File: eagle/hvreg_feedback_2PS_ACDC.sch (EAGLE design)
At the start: 20 parts

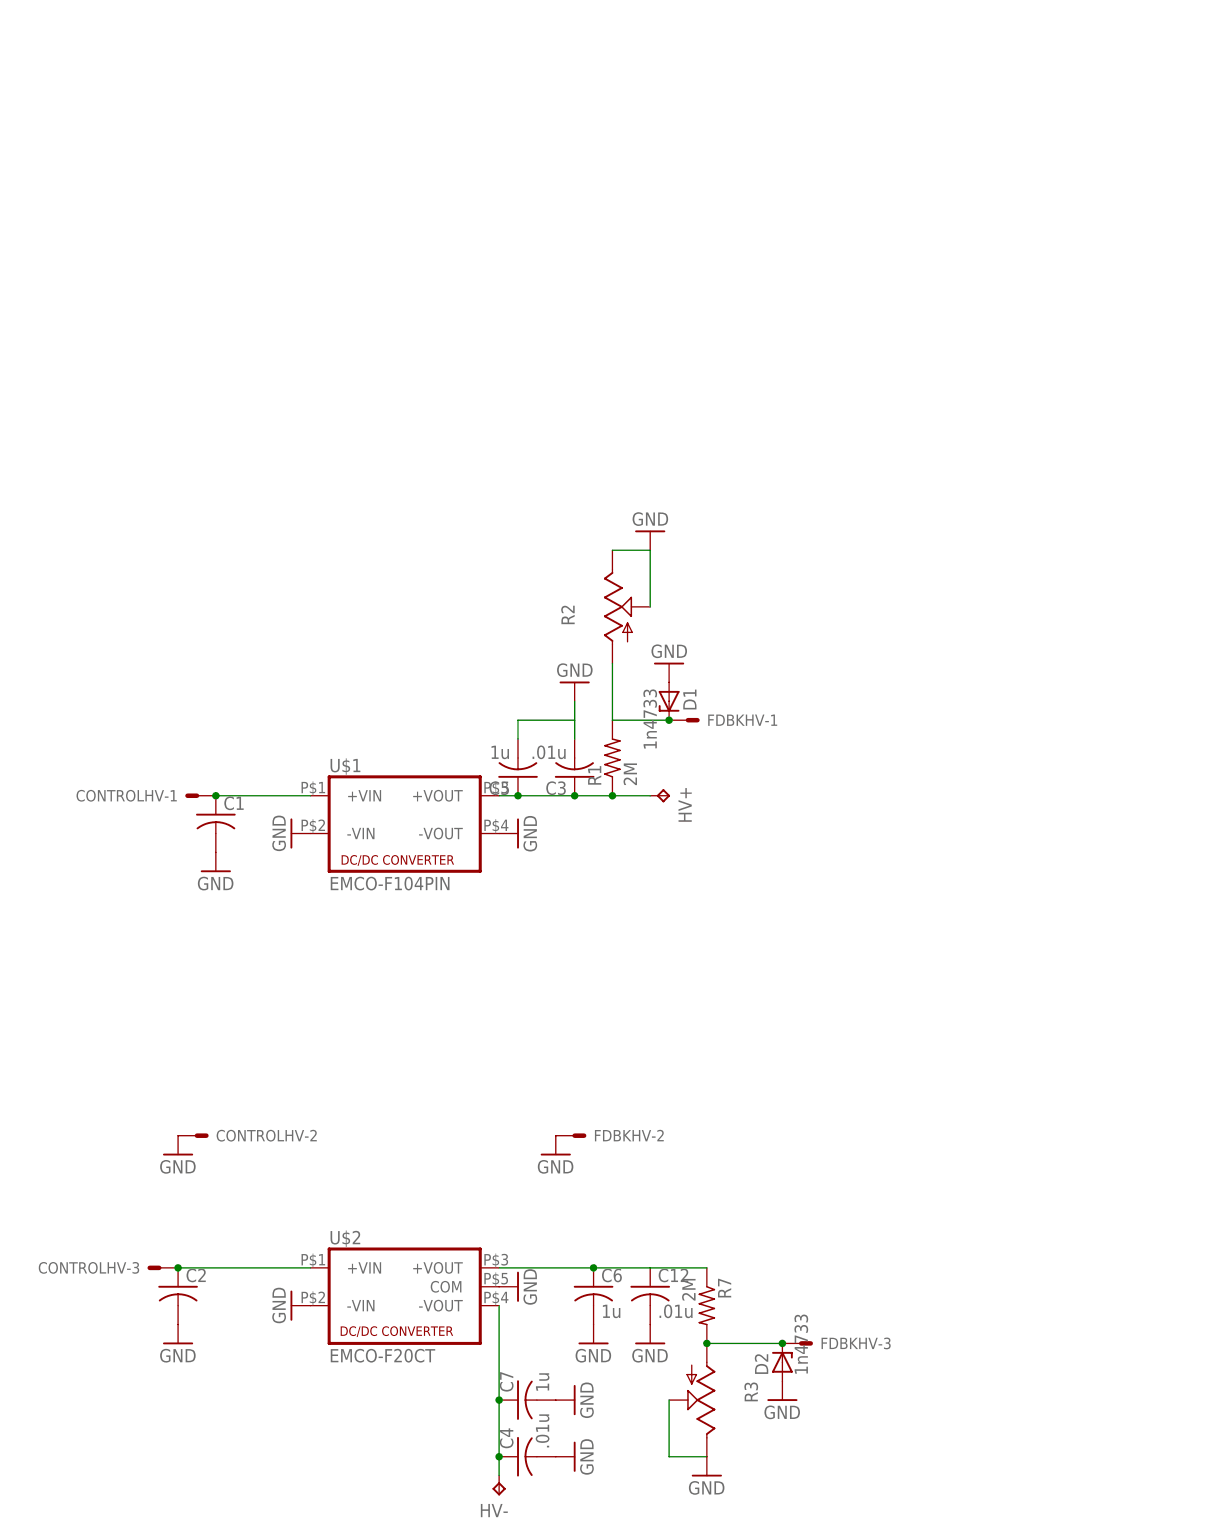
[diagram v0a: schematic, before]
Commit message: use SW on one side, DC on the other. HV feedback. Positive only
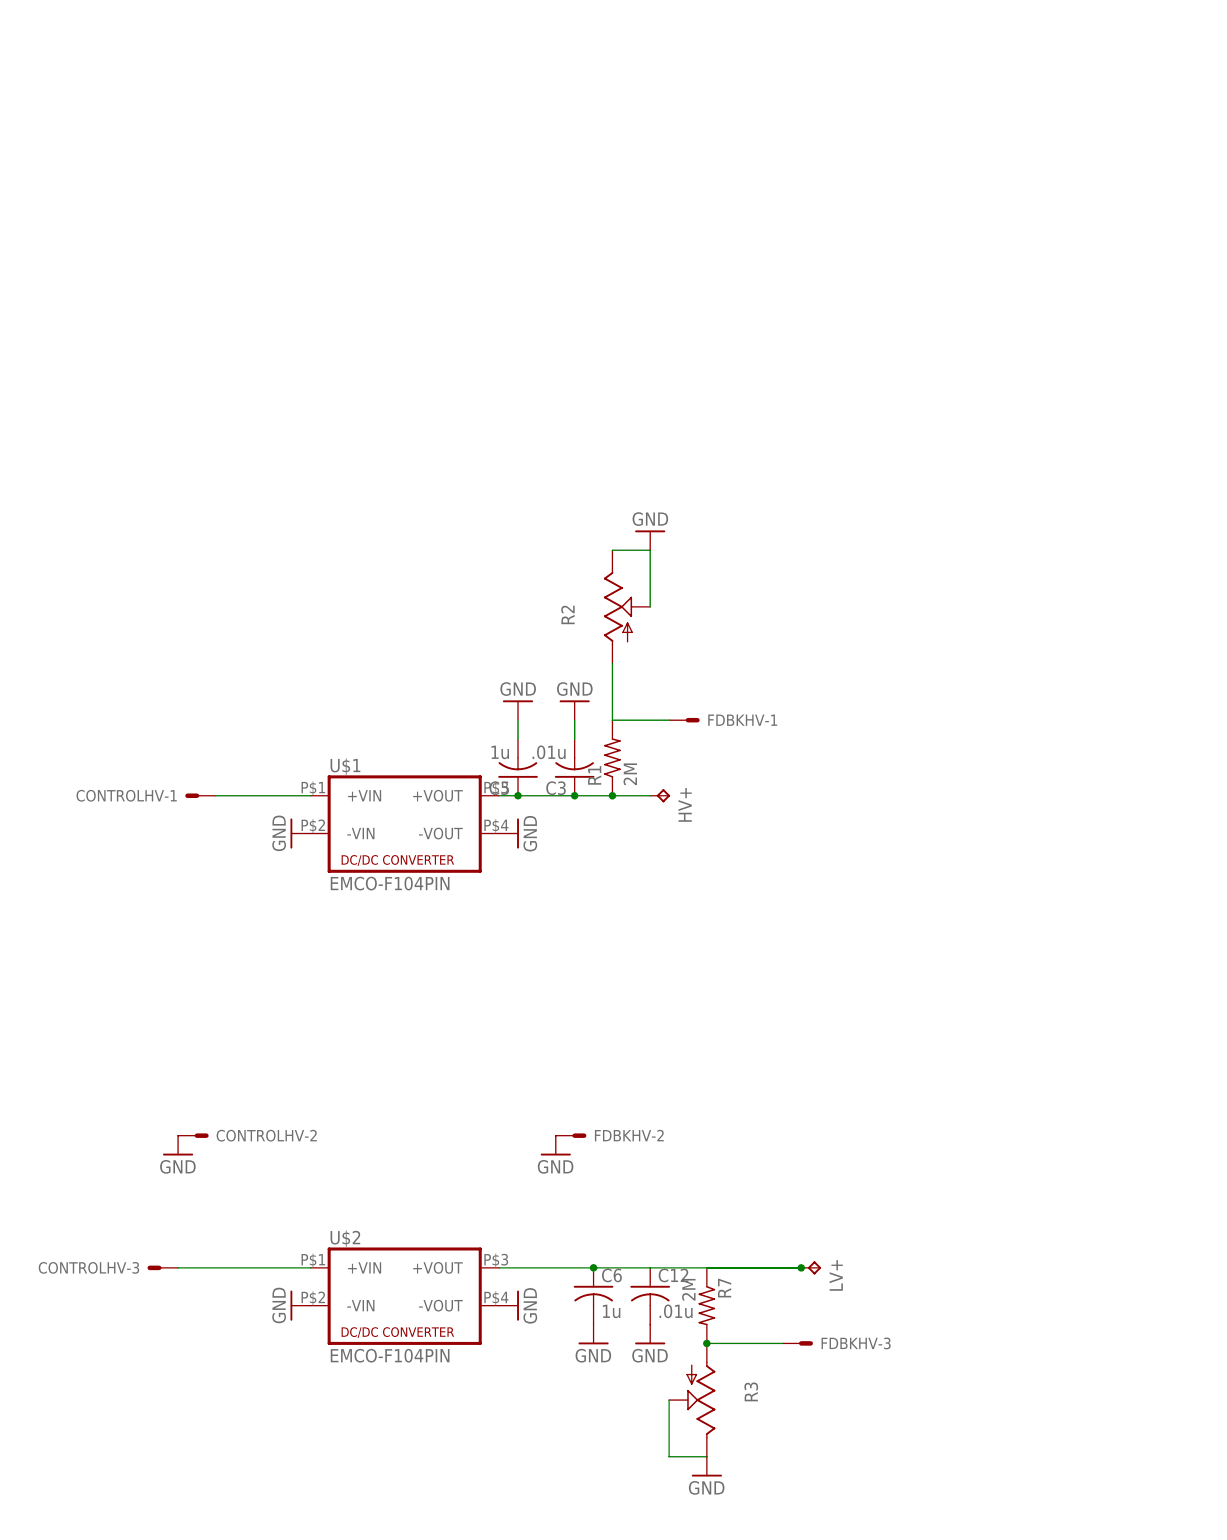
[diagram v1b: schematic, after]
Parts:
- removed C1, C2: (no value), rcl:C-US050-030X075
- removed C4: .01u, rcl:C-US075-042X103
- removed C7: 1u, rcl:C-US225-108X268
- removed D1, D2: 1n4733, diode:ZENER-DIODEZD-10
- removed HV-: TPPAD1-20Y, testpad:TPPAD1-20Y
- added LV+: TPPAD1-20Y, testpad:TPPAD1-20Y
- U$2: value EMCO-F20CT -> EMCO-F104PIN; device dc-dc-converter:EMCO-F20CT -> dc-dc-converter:EMCO-F104PIN
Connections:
- removed net N$6: C4.1, C7.1, HV-.TP, U$2.-VOUT
- net GND: now also U$2.-VOUT; no longer C1.2, C2.2, C4.2, C7.2, D1.A, D2.A, U$2.COM
- net N$2: now also LV+.TP
- net N$3: no longer D1.C
- net N$4: no longer C1.1
- net N$5: no longer C2.1
- net N$8: no longer D2.C
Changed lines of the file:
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@@
 <part name="GND6" library="supply1" deviceset="GND" device=""/>
 <part name="HV+" library="testpad" deviceset="TP" device="PAD1-20Y"/>
-<part name="HV-" library="testpad" deviceset="TP" device="PAD1-20Y"/>
 <part name="C3" library="rcl" deviceset="C-US" device="075-042X103" value=".01u"/>
 <part name="GND9" library="supply1" deviceset="GND" device=""/>
@@
 <part name="FDBKHV" library="con-molex" deviceset="KK-156-3" device=""/>
 <part name="GND3" library="supply1" deviceset="GND" device=""/>
-<part name="D1" library="diode" deviceset="ZENER-DIODE" device="ZD-10" value="1n4733"/>
-<part name="GND4" library="supply1" deviceset="GND" device=""/>
-<part name="D2" library="diode" deviceset="ZENER-DIODE" device="ZD-10" value="1n4733"/>
-<part name="GND8" library="supply1" deviceset="GND" device=""/>
-<part name="C1" library="rcl" deviceset="C-US" device="050-030X075"/>
-<part name="C2" library="rcl" deviceset="C-US" device="050-030X075"/>
-<part name="GND10" library="supply1" deviceset="GND" device=""/>
-<part name="GND11" library="supply1" deviceset="GND" device=""/>
-<part name="U$2" library="dc-dc-converter" deviceset="EMCO-F20CT" device=""/>
 <part name="GND7" library="supply1" deviceset="GND" device=""/>
-<part name="C4" library="rcl" deviceset="C-US" device="075-042X103" value=".01u"/>
-<part name="GND13" library="supply1" deviceset="GND" device=""/>
 <part name="R2" library="pot" deviceset="TRIM_US-" device="B90P"/>
 <part name="R3" library="pot" deviceset="TRIM_US-" device="B90P"/>
 <part name="C5" library="rcl" deviceset="C-US" device="225-108X268" value="1u"/>
 <part name="C6" library="rcl" deviceset="C-US" device="225-108X268" value="1u"/>
-<part name="C7" library="rcl" deviceset="C-US" device="225-108X268" value="1u"/>
-<part name="GND14" library="supply1" deviceset="GND" device=""/>
 <part name="GND16" library="supply1" deviceset="GND" device=""/>
+<part name="LV+" library="testpad" deviceset="TP" device="PAD1-20Y"/>
+<part name="U$2" library="dc-dc-converter" deviceset="EMCO-F10" device="4PIN"/>
+<part name="GND4" library="supply1" deviceset="GND" device=""/>
 </parts>
 <sheets>
@@
 <instance part="GND6" gate="1" x="63.5" y="48.26" rot="R90"/>
 <instance part="HV+" gate="G$1" x="83.82" y="53.34" rot="R270"/>
-<instance part="HV-" gate="G$1" x="60.96" y="-40.64" rot="R180"/>
 <instance part="C3" gate="G$1" x="71.12" y="55.88" rot="R180"/>
-<instance part="GND9" gate="1" x="71.12" y="68.58" rot="R180"/>
+<instance part="GND9" gate="1" x="71.12" y="66.04" rot="R180"/>
 <instance part="GND17" gate="1" x="81.28" y="-20.32"/>
 <instance part="C12" gate="G$1" x="81.28" y="-12.7"/>
@@
 <instance part="FDBKHV" gate="-3" x="101.6" y="-20.32"/>
 <instance part="GND3" gate="1" x="17.78" y="5.08"/>
-<instance part="D1" gate="G$1" x="83.82" y="66.04" rot="R270"/>
-<instance part="GND4" gate="1" x="83.82" y="71.12" rot="R180"/>
-<instance part="D2" gate="G$1" x="99.06" y="-22.86" rot="R90"/>
-<instance part="GND8" gate="1" x="99.06" y="-27.94"/>
-<instance part="C1" gate="G$1" x="22.86" y="50.8"/>
-<instance part="C2" gate="G$1" x="17.78" y="-12.7"/>
-<instance part="GND10" gate="1" x="17.78" y="-20.32"/>
-<instance part="GND11" gate="1" x="22.86" y="43.18"/>
-<instance part="U$2" gate="G$1" x="48.26" y="-12.7"/>
-<instance part="GND7" gate="1" x="63.5" y="-12.7" rot="R90"/>
-<instance part="C4" gate="G$1" x="63.5" y="-35.56" rot="R90"/>
-<instance part="GND13" gate="1" x="71.12" y="-35.56" rot="R90"/>
+<instance part="GND7" gate="1" x="63.5" y="-15.24" rot="R90"/>
 <instance part="R2" gate="G$1" x="76.2" y="78.74"/>
 <instance part="R3" gate="G$1" x="88.9" y="-27.94" rot="R180"/>
 <instance part="C5" gate="G$1" x="63.5" y="55.88" rot="R180"/>
 <instance part="C6" gate="G$1" x="73.66" y="-12.7"/>
-<instance part="C7" gate="G$1" x="63.5" y="-27.94" rot="R90"/>
-<instance part="GND14" gate="1" x="71.12" y="-27.94" rot="R90"/>
 <instance part="GND16" gate="1" x="73.66" y="-20.32"/>
+<instance part="LV+" gate="G$1" x="104.14" y="-10.16" rot="R270"/>
+<instance part="U$2" gate="G$1" x="48.26" y="-12.7"/>
+<instance part="GND4" gate="1" x="63.5" y="66.04" rot="R180"/>
 </instances>
 <busses>
@@
 <pinref part="C3" gate="G$1" pin="2"/>
 <pinref part="GND9" gate="1" pin="GND"/>
-<wire x1="71.12" y1="66.04" x2="71.12" y2="63.5" width="0.1524" layer="91"/>
 <wire x1="71.12" y1="63.5" x2="71.12" y2="60.96" width="0.1524" layer="91"/>
-<wire x1="71.12" y1="63.5" x2="63.5" y2="63.5" width="0.1524" layer="91"/>
-<pinref part="C5" gate="G$1" pin="2"/>
-<wire x1="63.5" y1="63.5" x2="63.5" y2="60.96" width="0.1524" layer="91"/>
 </segment>
 <segment>
@@
 <pinref part="CONTROLHV" gate="-2" pin="S"/>
 <pinref part="GND3" gate="1" pin="GND"/>
-</segment>
-<segment>
-<pinref part="D1" gate="G$1" pin="A"/>
-<pinref part="GND4" gate="1" pin="GND"/>
-</segment>
-<segment>
-<pinref part="D2" gate="G$1" pin="A"/>
-<pinref part="GND8" gate="1" pin="GND"/>
-</segment>
-<segment>
-<pinref part="C2" gate="G$1" pin="2"/>
-<pinref part="GND10" gate="1" pin="GND"/>
-</segment>
-<segment>
-<pinref part="C1" gate="G$1" pin="2"/>
-<pinref part="GND11" gate="1" pin="GND"/>
-</segment>
-<segment>
-<pinref part="GND1" gate="1" pin="GND"/>
-<pinref part="U$2" gate="G$1" pin="-VIN"/>
-</segment>
-<segment>
-<pinref part="U$2" gate="G$1" pin="COM"/>
-<pinref part="GND7" gate="1" pin="GND"/>
-</segment>
-<segment>
-<pinref part="C4" gate="G$1" pin="2"/>
-<pinref part="GND13" gate="1" pin="GND"/>
 </segment>
 <segment>
@@
 </segment>
 <segment>
-<pinref part="C7" gate="G$1" pin="2"/>
-<pinref part="GND14" gate="1" pin="GND"/>
+<pinref part="C6" gate="G$1" pin="2"/>
+<pinref part="GND16" gate="1" pin="GND"/>
 </segment>
 <segment>
-<pinref part="C6" gate="G$1" pin="2"/>
-<pinref part="GND16" gate="1" pin="GND"/>
+<pinref part="GND7" gate="1" pin="GND"/>
+<pinref part="U$2" gate="G$1" pin="-VOUT"/>
+</segment>
+<segment>
+<pinref part="GND1" gate="1" pin="GND"/>
+<pinref part="U$2" gate="G$1" pin="-VIN"/>
+</segment>
+<segment>
+<pinref part="C5" gate="G$1" pin="2"/>
+<wire x1="63.5" y1="63.5" x2="63.5" y2="60.96" width="0.1524" layer="91"/>
+<pinref part="GND4" gate="1" pin="GND"/>
 </segment>
 </net>
@@
 <segment>
 <pinref part="C12" gate="G$1" pin="1"/>
-<wire x1="81.28" y1="-10.16" x2="88.9" y2="-10.16" width="0.1524" layer="91"/>
+<wire x1="81.28" y1="-10.16" x2="101.6" y2="-10.16" width="0.1524" layer="91"/>
 <pinref part="R7" gate="G$1" pin="1"/>
-<pinref part="U$2" gate="G$1" pin="+VOUT"/>
 <wire x1="81.28" y1="-10.16" x2="73.66" y2="-10.16" width="0.1524" layer="91"/>
 <pinref part="C6" gate="G$1" pin="1"/>
 <wire x1="73.66" y1="-10.16" x2="60.96" y2="-10.16" width="0.1524" layer="91"/>
 <junction x="73.66" y="-10.16"/>
+<pinref part="LV+" gate="G$1" pin="TP"/>
+<junction x="101.6" y="-10.16"/>
+<wire x1="101.6" y1="-10.16" x2="88.9" y2="-10.16" width="0.1524" layer="91"/>
+<pinref part="U$2" gate="G$1" pin="+VOUT"/>
 </segment>
 </net>
@@
 <pinref part="FDBKHV" gate="-1" pin="S"/>
 <wire x1="83.82" y1="63.5" x2="76.2" y2="63.5" width="0.1524" layer="91"/>
-<pinref part="D1" gate="G$1" pin="C"/>
-<junction x="83.82" y="63.5"/>
 <pinref part="R2" gate="G$1" pin="A"/>
 <wire x1="76.2" y1="63.5" x2="76.2" y2="71.12" width="0.1524" layer="91"/>
@@
 <pinref part="FDBKHV" gate="-3" pin="S"/>
 <wire x1="99.06" y1="-20.32" x2="88.9" y2="-20.32" width="0.1524" layer="91"/>
-<pinref part="D2" gate="G$1" pin="C"/>
-<junction x="99.06" y="-20.32"/>
 <pinref part="R3" gate="G$1" pin="A"/>
 <junction x="88.9" y="-20.32"/>
@@
 <pinref part="CONTROLHV" gate="-1" pin="S"/>
 <wire x1="22.86" y1="53.34" x2="35.56" y2="53.34" width="0.1524" layer="91"/>
-<pinref part="C1" gate="G$1" pin="1"/>
-<junction x="22.86" y="53.34"/>
 </segment>
 </net>
@@
 <pinref part="CONTROLHV" gate="-3" pin="S"/>
 <wire x1="17.78" y1="-10.16" x2="35.56" y2="-10.16" width="0.1524" layer="91"/>
-<pinref part="C2" gate="G$1" pin="1"/>
-<junction x="17.78" y="-10.16"/>
 <pinref part="U$2" gate="G$1" pin="+VIN"/>
 </segment>
 </net>
-<net name="N$6" class="0">
-<segment>
-<pinref part="U$2" gate="G$1" pin="-VOUT"/>
-<pinref part="HV-" gate="G$1" pin="TP"/>
-<wire x1="60.96" y1="-35.56" x2="60.96" y2="-27.94" width="0.1524" layer="91"/>
-<pinref part="C4" gate="G$1" pin="1"/>
-<junction x="60.96" y="-35.56"/>
-<pinref part="C7" gate="G$1" pin="1"/>
-<wire x1="60.96" y1="-27.94" x2="60.96" y2="-15.24" width="0.1524" layer="91"/>
-<junction x="60.96" y="-27.94"/>
-<wire x1="60.96" y1="-35.56" x2="60.96" y2="-38.1" width="0.1524" layer="91"/>
-</segment>
-</net>

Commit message: capacitor bank
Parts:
- added C1, C4: 1n, rcl:C-US075-042X103
- added C2, C7: 10p, rcl:C-US075-042X103
- C5, C6: device rcl:C-US225-108X268 -> rcl:C-US275-205X316
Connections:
- net GND: now also C1.2, C2.2, C4.2, C7.2
- net N$1: now also C1.1, C2.1
- net N$2: now also C4.1, C7.1
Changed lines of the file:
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@@
 <part name="R2" library="pot" deviceset="TRIM_US-" device="B90P"/>
 <part name="R3" library="pot" deviceset="TRIM_US-" device="B90P"/>
-<part name="C5" library="rcl" deviceset="C-US" device="225-108X268" value="1u"/>
-<part name="C6" library="rcl" deviceset="C-US" device="225-108X268" value="1u"/>
+<part name="C5" library="rcl" deviceset="C-US" device="275-205X316" value="1u"/>
+<part name="C6" library="rcl" deviceset="C-US" device="275-205X316" value="1u"/>
 <part name="GND16" library="supply1" deviceset="GND" device=""/>
 <part name="LV+" library="testpad" deviceset="TP" device="PAD1-20Y"/>
 <part name="U$2" library="dc-dc-converter" deviceset="EMCO-F10" device="4PIN"/>
 <part name="GND4" library="supply1" deviceset="GND" device=""/>
+<part name="C1" library="rcl" deviceset="C-US" device="075-042X103" value="1n"/>
+<part name="C2" library="rcl" deviceset="C-US" device="075-042X103" value="10p"/>
+<part name="GND8" library="supply1" deviceset="GND" device=""/>
+<part name="GND10" library="supply1" deviceset="GND" device=""/>
+<part name="C4" library="rcl" deviceset="C-US" device="075-042X103" value="1n"/>
+<part name="C7" library="rcl" deviceset="C-US" device="075-042X103" value="10p"/>
+<part name="GND11" library="supply1" deviceset="GND" device=""/>
+<part name="GND13" library="supply1" deviceset="GND" device=""/>
 </parts>
 <sheets>
@@
 <instance part="U$2" gate="G$1" x="48.26" y="-12.7"/>
 <instance part="GND4" gate="1" x="63.5" y="66.04" rot="R180"/>
+<instance part="C1" gate="G$1" x="71.12" y="50.8"/>
+<instance part="C2" gate="G$1" x="76.2" y="50.8"/>
+<instance part="GND8" gate="1" x="71.12" y="43.18"/>
+<instance part="GND10" gate="1" x="76.2" y="43.18"/>
+<instance part="C4" gate="G$1" x="81.28" y="-7.62" rot="R180"/>
+<instance part="C7" gate="G$1" x="73.66" y="-7.62" rot="R180"/>
+<instance part="GND11" gate="1" x="81.28" y="0" rot="R180"/>
+<instance part="GND13" gate="1" x="73.66" y="0" rot="R180"/>
 </instances>
 <busses>
@@
 <pinref part="GND4" gate="1" pin="GND"/>
 </segment>
+<segment>
+<pinref part="C1" gate="G$1" pin="2"/>
+<pinref part="GND8" gate="1" pin="GND"/>
+</segment>
+<segment>
+<pinref part="C2" gate="G$1" pin="2"/>
+<pinref part="GND10" gate="1" pin="GND"/>
+</segment>
+<segment>
+<pinref part="C4" gate="G$1" pin="2"/>
+<pinref part="GND11" gate="1" pin="GND"/>
+</segment>
+<segment>
+<pinref part="C7" gate="G$1" pin="2"/>
+<pinref part="GND13" gate="1" pin="GND"/>
+</segment>
 </net>
 <net name="N$1" class="0">
@@
 <junction x="63.5" y="53.34"/>
 <wire x1="63.5" y1="53.34" x2="60.96" y2="53.34" width="0.1524" layer="91"/>
+<pinref part="C1" gate="G$1" pin="1"/>
+<pinref part="C2" gate="G$1" pin="1"/>
 </segment>
 </net>
@@
 <wire x1="101.6" y1="-10.16" x2="88.9" y2="-10.16" width="0.1524" layer="91"/>
 <pinref part="U$2" gate="G$1" pin="+VOUT"/>
+<pinref part="C4" gate="G$1" pin="1"/>
+<junction x="81.28" y="-10.16"/>
+<pinref part="C7" gate="G$1" pin="1"/>
 </segment>
 </net>

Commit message: IXYS board solution, gatedriver components
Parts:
- added D1, D2: 1N4004, diode:1N4004
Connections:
- new net N$6: D1.C, HV+.TP
- new net N$7: D2.C, LV+.TP
- net N$1: now also D1.A; no longer HV+.TP
- net N$2: now also D2.A; no longer LV+.TP
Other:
- moved on the sheet: HV+
